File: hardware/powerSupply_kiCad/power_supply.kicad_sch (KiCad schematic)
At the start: 23 parts, among them IC1 LT7101EUHE-PBF, J1 CLCK, J2 MODE, J3 436500201, J4 436500201

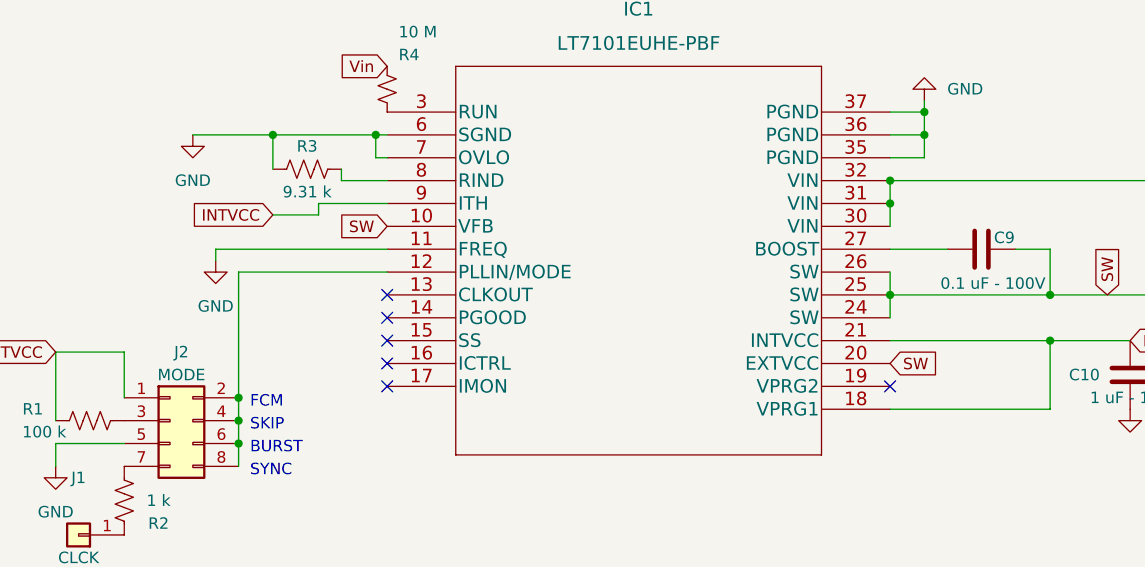
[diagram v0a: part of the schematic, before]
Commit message: Verification of all pins of the LT7101
According to the datasheet and DC2895A demoboard
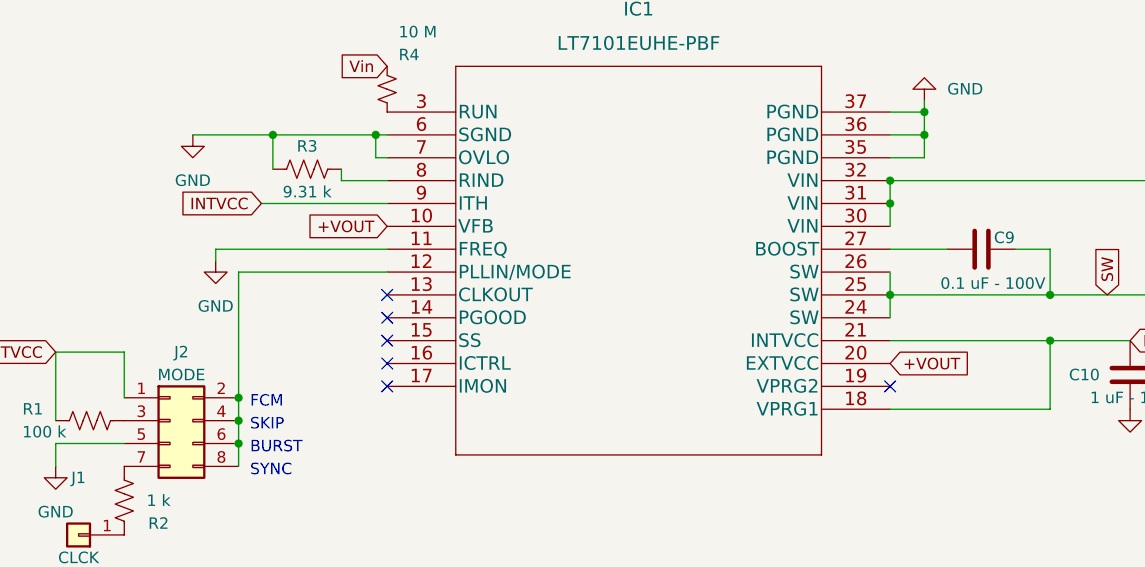
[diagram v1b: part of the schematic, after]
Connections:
- net +VOUT: now also IC1.10 (VFB), IC1.20 (EXTVCC)
- net SW: no longer IC1.10 (VFB), IC1.20 (EXTVCC)
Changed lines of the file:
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@@
     (stroke (width 0) (type default) (color 0 0 0 0))
   )
-  (wire (pts (xy 133.35 60.96) (xy 133.35 62.23))
+  (wire (pts (xy 127 60.96) (xy 140.97 60.96))
     (stroke (width 0) (type default) (color 0 0 0 0))
   )
@@
     (stroke (width 0) (type default) (color 0 0 0 0))
   )
-  (wire (pts (xy 133.35 62.23) (xy 128.27 62.23))
-    (stroke (width 0) (type default) (color 0 0 0 0))
-  )
-  (wire (pts (xy 140.97 60.96) (xy 133.35 60.96))
-    (stroke (width 0) (type default) (color 0 0 0 0))
-  )
   (wire (pts (xy 196.85 60.96) (xy 196.85 63.5))
     (stroke (width 0) (type default) (color 0 0 0 0))
@@
     )
   )
-  (global_label "SW" (shape input) (at 196.85 78.74 0) (fields_autoplaced)
-    (effects (font (size 1.27 1.27)) (justify left))
-    (property "Intersheet References" "${INTERSHEET_REFS}" (id 0) (at 201.9241 78.6606 0)
-      (effects (font (size 1.27 1.27)) (justify left) hide)
-    )
-  )
-  (global_label "INTVCC" (shape input) (at 128.27 62.23 180) (fields_autoplaced)
-    (effects (font (size 1.27 1.27)) (justify right))
-    (property "Intersheet References" "${INTERSHEET_REFS}" (id 0) (at 119.3255 62.1506 0)
+  (global_label "INTVCC" (shape input) (at 127 60.96 180) (fields_autoplaced)
+    (effects (font (size 1.27 1.27)) (justify right))
+    (property "Intersheet References" "${INTERSHEET_REFS}" (id 0) (at 118.0555 60.8806 0)
       (effects (font (size 1.27 1.27)) (justify right) hide)
     )
@@
     )
   )
-  (global_label "SW" (shape input) (at 140.97 63.5 180) (fields_autoplaced)
-    (effects (font (size 1.27 1.27)) (justify right))
-    (property "Intersheet References" "${INTERSHEET_REFS}" (id 0) (at 135.8959 63.4206 0)
-      (effects (font (size 1.27 1.27)) (justify right) hide)
-    )
-  )
   (global_label "Vin" (shape input) (at 234.95 58.42 0) (fields_autoplaced)
     (effects (font (size 1.27 1.27)) (justify left))
@@
     )
   )
+  (global_label "+VOUT" (shape input) (at 196.85 78.74 0) (fields_autoplaced)
+    (effects (font (size 1.27 1.27)) (justify left))
+    (property "Intersheet References" "${INTERSHEET_REFS}" (id 0) (at 205.5526 78.6606 0)
+      (effects (font (size 1.27 1.27)) (justify left) hide)
+    )
+  )
   (global_label "Vbb" (shape input) (at 39.37 46.99 180) (fields_autoplaced)
     (effects (font (size 1.27 1.27)) (justify right))
@@
     )
   )
+  (global_label "+VOUT" (shape input) (at 140.97 63.5 180) (fields_autoplaced)
+    (effects (font (size 1.27 1.27)) (justify right))
+    (property "Intersheet References" "${INTERSHEET_REFS}" (id 0) (at 132.2674 63.5794 0)
+      (effects (font (size 1.27 1.27)) (justify right) hide)
+    )
+  )

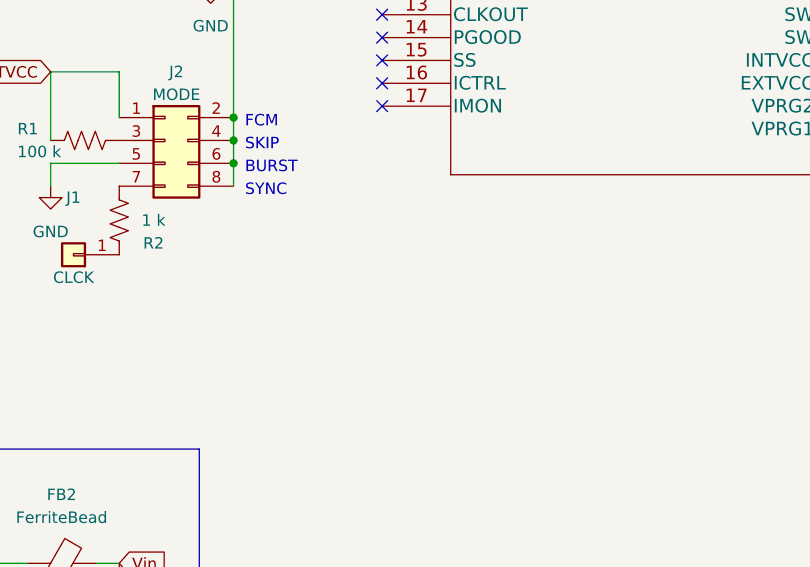
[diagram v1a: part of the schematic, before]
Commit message: Added M3 via and GNd pin
Reshape for 35 mm width
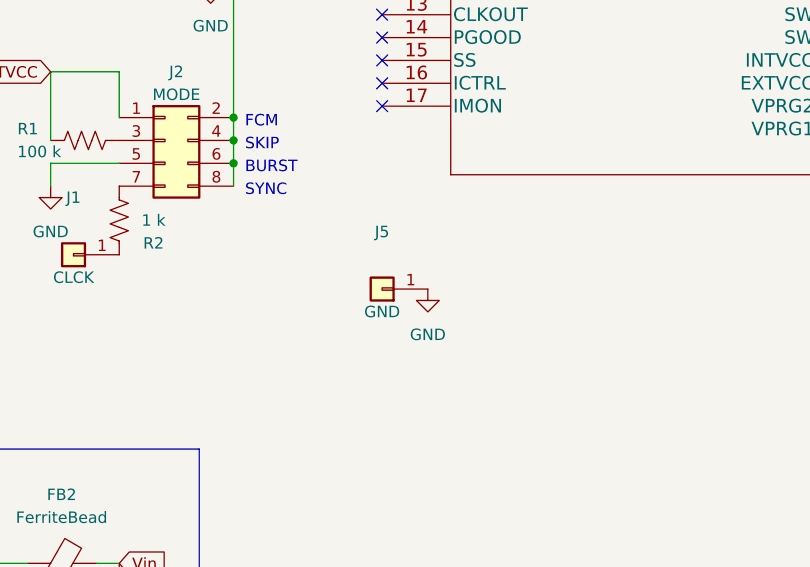
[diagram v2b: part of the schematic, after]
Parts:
- added J5: GND, Connector_PinHeader_2.54mm:PinHeader_1x01_P2.54mm_Vertical, symbol Connector_Generic:Conn_01x01
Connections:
- net GND: now also J5.1 (Pin_1)
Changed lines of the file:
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@@
+    (pin "1")
+  )
+  (symbol (lib_id "Connector_Generic:Conn_01x01") (at 140.97 101.6 180) (unit 1)
+    (in_bom yes) (on_board yes)
+    (property "Reference" "J5" (id 0) (at 140.97 95.25 0))
+    (property "Value" "GND" (id 1) (at 140.97 104.14 0))
+    (property "Footprint" "Connector_PinHeader_2.54mm:PinHeader_1x01_P2.54mm_Vertical" (id 2) (at 140.97 101.6 0)
+      (effects (font (size 1.27 1.27)) hide)
+    )
+    (property "Datasheet" "~" (id 3) (at 140.97 101.6 0)
+      (effects (font (size 1.27 1.27)) hide)
+    )
     (pin "1")
   )
@@
     (pin "2")
   )
+  (symbol (lib_id "power:GND") (at 146.05 101.6 0) (unit 1)
+    (in_bom yes) (on_board yes) (fields_autoplaced)
+    (property "Reference" "#PWR09" (id 0) (at 146.05 107.95 0)
+      (effects (font (size 1.27 1.27)) hide)
+    )
+    (property "Value" "GND" (id 1) (at 146.05 106.68 0))
+    (property "Footprint" "" (id 2) (at 146.05 101.6 0)
+      (effects (font (size 1.27 1.27)) hide)
+    )
+    (property "Datasheet" "" (id 3) (at 146.05 101.6 0)
+      (effects (font (size 1.27 1.27)) hide)
+    )
+    (pin "1")
+  )
   (sheet_instances
     (path "/" (page "1"))
@@
       (reference "#PWR08") (unit 1) (value "GND") (footprint "")
     )
+    (path "/ebb79beb-057b-491f-b139-bfb12998428a"
+      (reference "#PWR09") (unit 1) (value "GND") (footprint "")
+    )
     (path "/b68af152-3497-40fe-8dd2-bb24ba4a19ed"
       (reference "C4") (unit 1) (value "4.7 uF - 100V") (footprint "Capacitor_SMD:C_1210_3225Metric")
@@
       (reference "J4") (unit 1) (value "436500201") (footprint "bib:436500201")
     )
+    (path "/52b4048a-2ed2-456e-bb7d-9dac3c1fa093"
+      (reference "J5") (unit 1) (value "GND") (footprint "Connector_PinHeader_2.54mm:PinHeader_1x01_P2.54mm_Vertical")
+    )
     (path "/cd38f80d-e974-4c5b-bf19-e95abde91961"
